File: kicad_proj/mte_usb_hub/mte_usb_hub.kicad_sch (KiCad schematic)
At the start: 22 parts

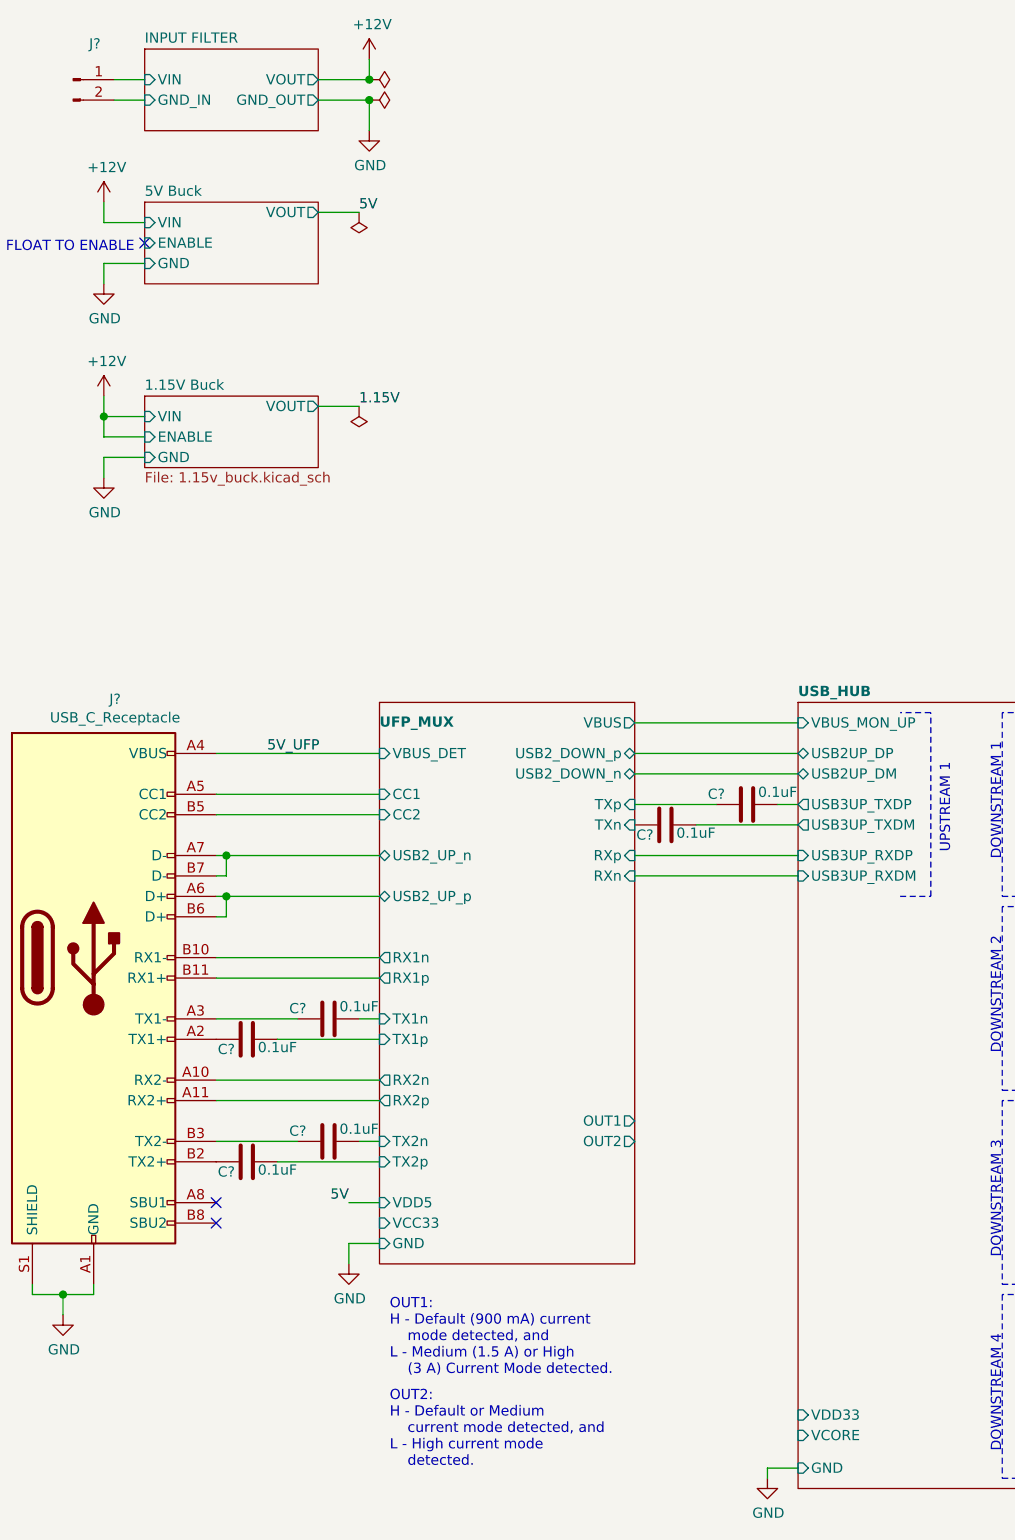
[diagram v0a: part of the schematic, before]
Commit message: Adds 3v3 LDO
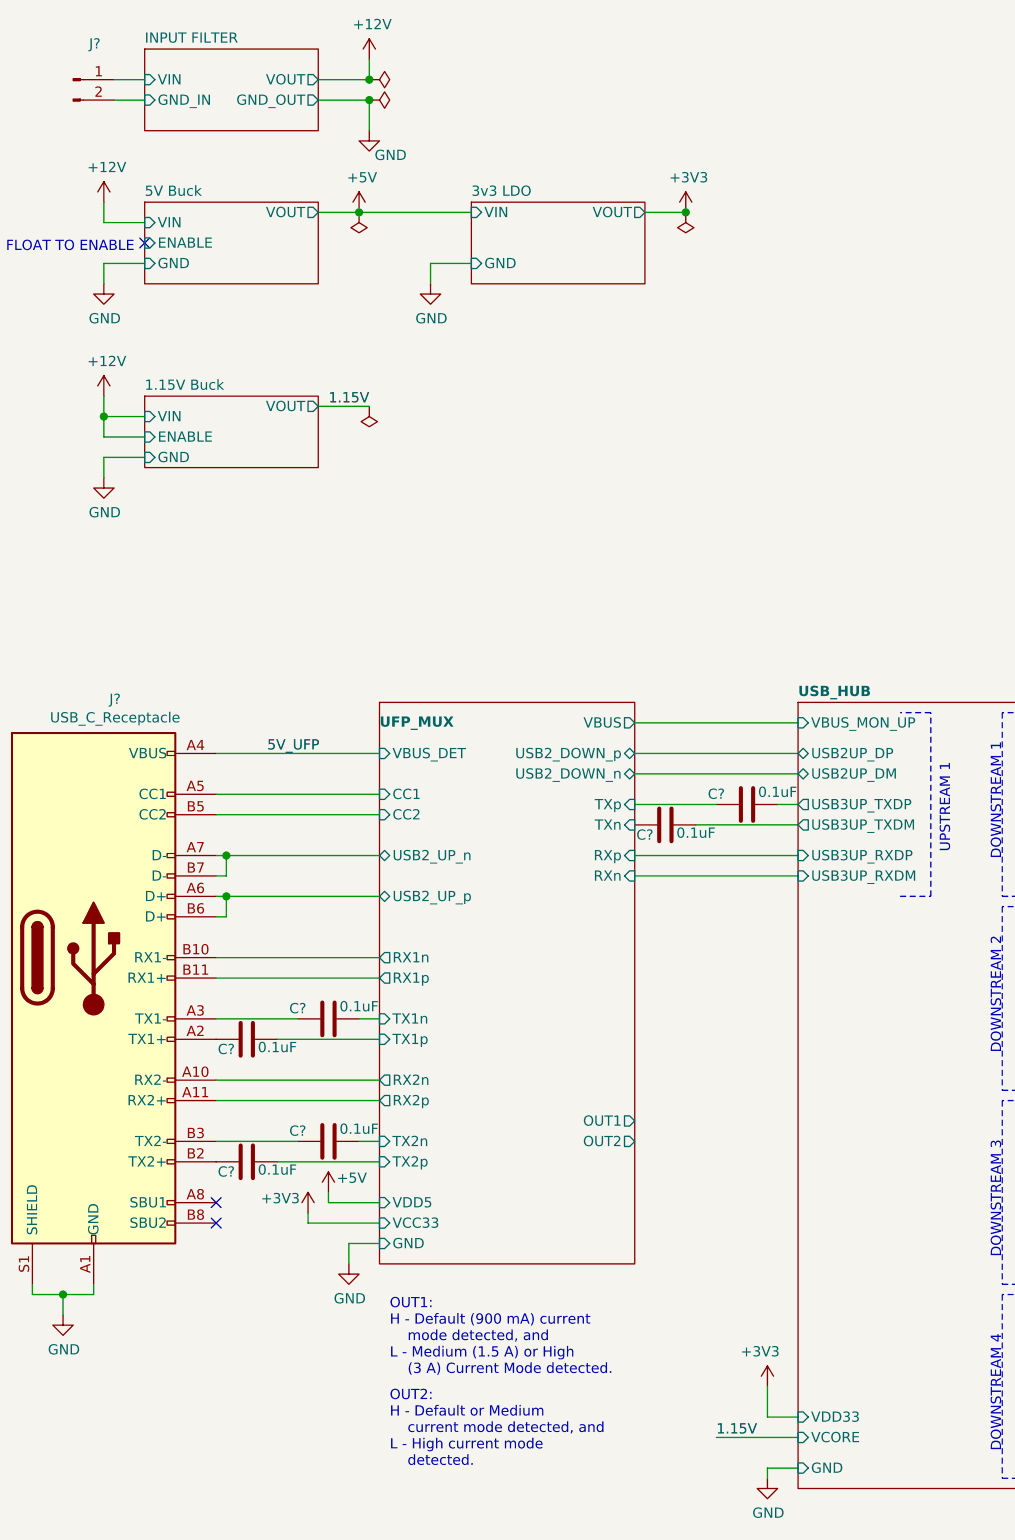
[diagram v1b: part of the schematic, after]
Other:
- added sheet 3v3 LDO (3v3_ldo.kicad_sch)

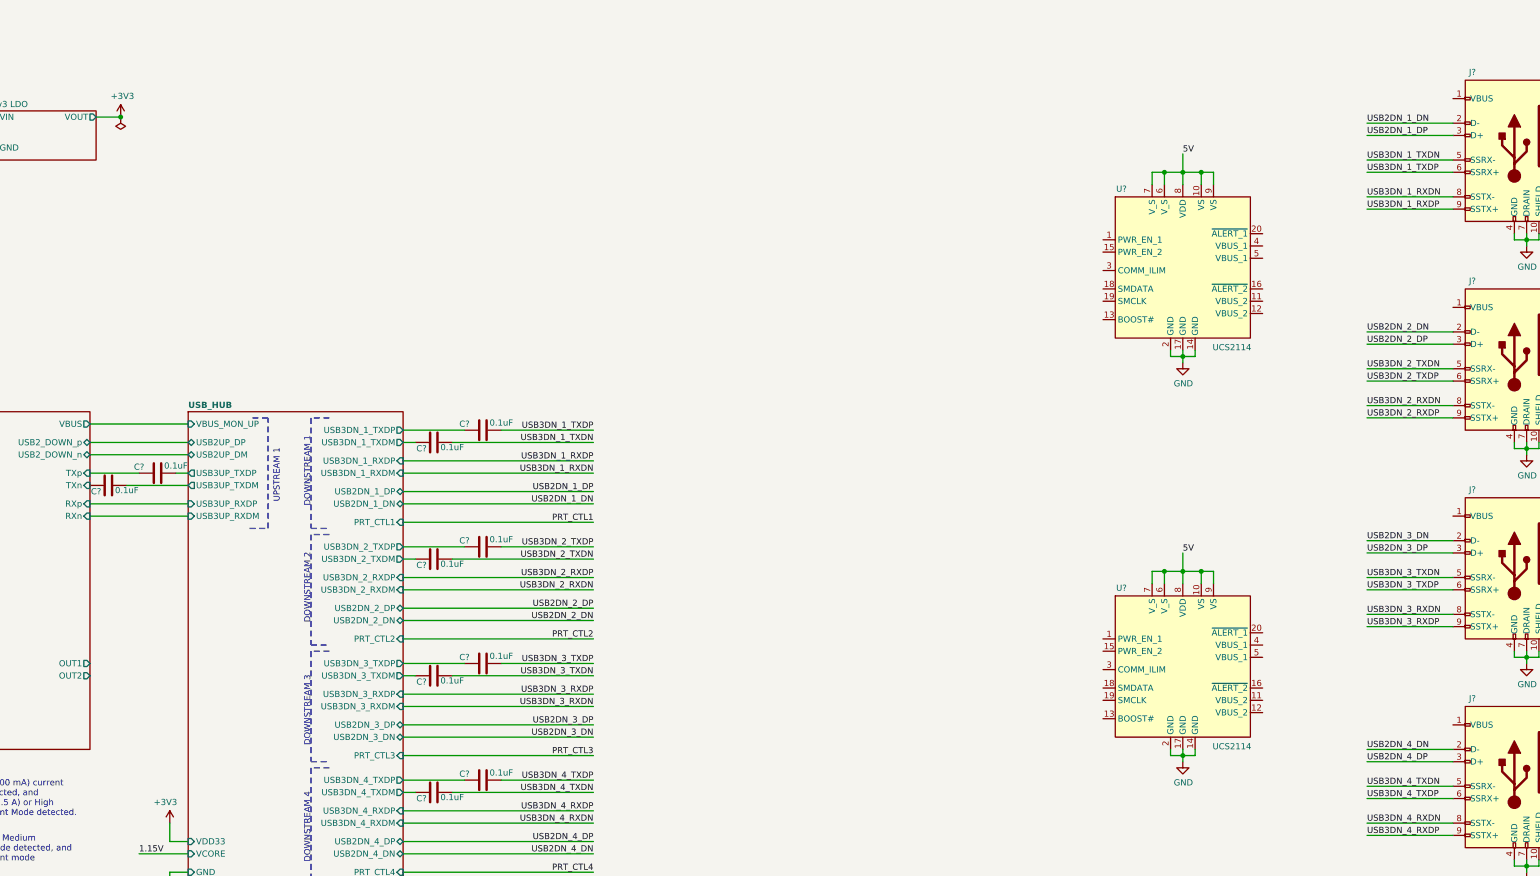
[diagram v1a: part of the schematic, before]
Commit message: Implements VBUS monitor, starts ESD protection
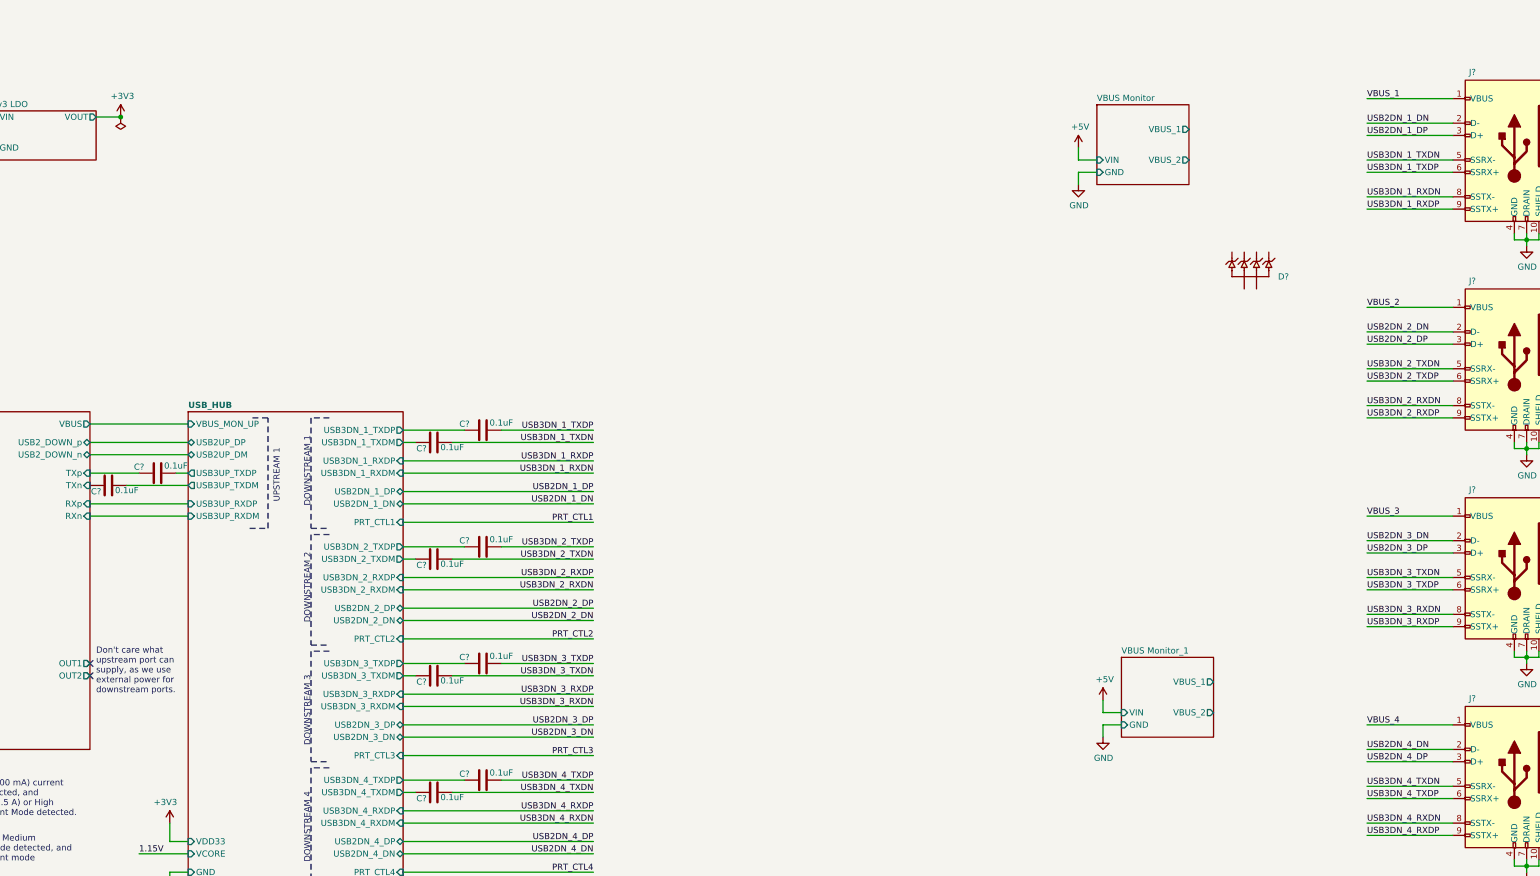
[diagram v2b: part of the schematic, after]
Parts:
- removed U? (x2): UCS2114, symbol mte_usb_hub:UCS2114
- added D?: ESD8004MUTAG, symbol mte_usb_hub:ESD8004MUTAG
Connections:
- net VBUS_3: now reaches J?.1 (VBUS)
- net VBUS_2: now reaches J?.1 (VBUS)
- net VBUS_1: now reaches J?.1 (VBUS)
- net VBUS_4: now reaches J?.1 (VBUS)
- no-connect marks 3 -> 5
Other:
- added sheet VBUS Monitor (vbus_monitor.kicad_sch)
- added sheet VBUS Monitor_1 (vbus_monitor.kicad_sch)
- note added: "Don't care what upstream port can supply, as we use external power for downstream ports."

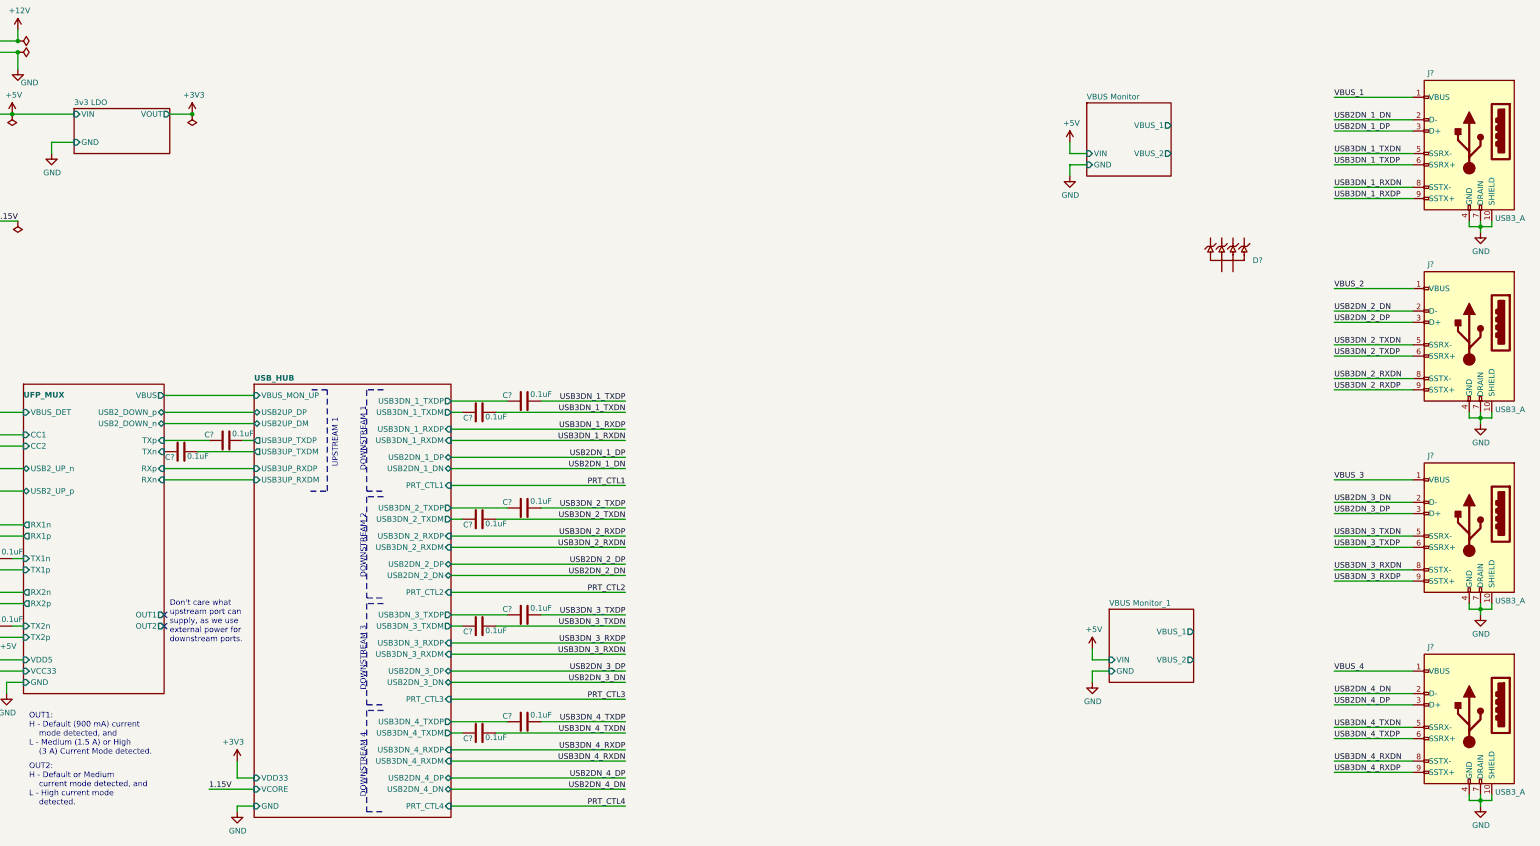
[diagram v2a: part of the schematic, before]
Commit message: Finishes input filter, minor buck changes
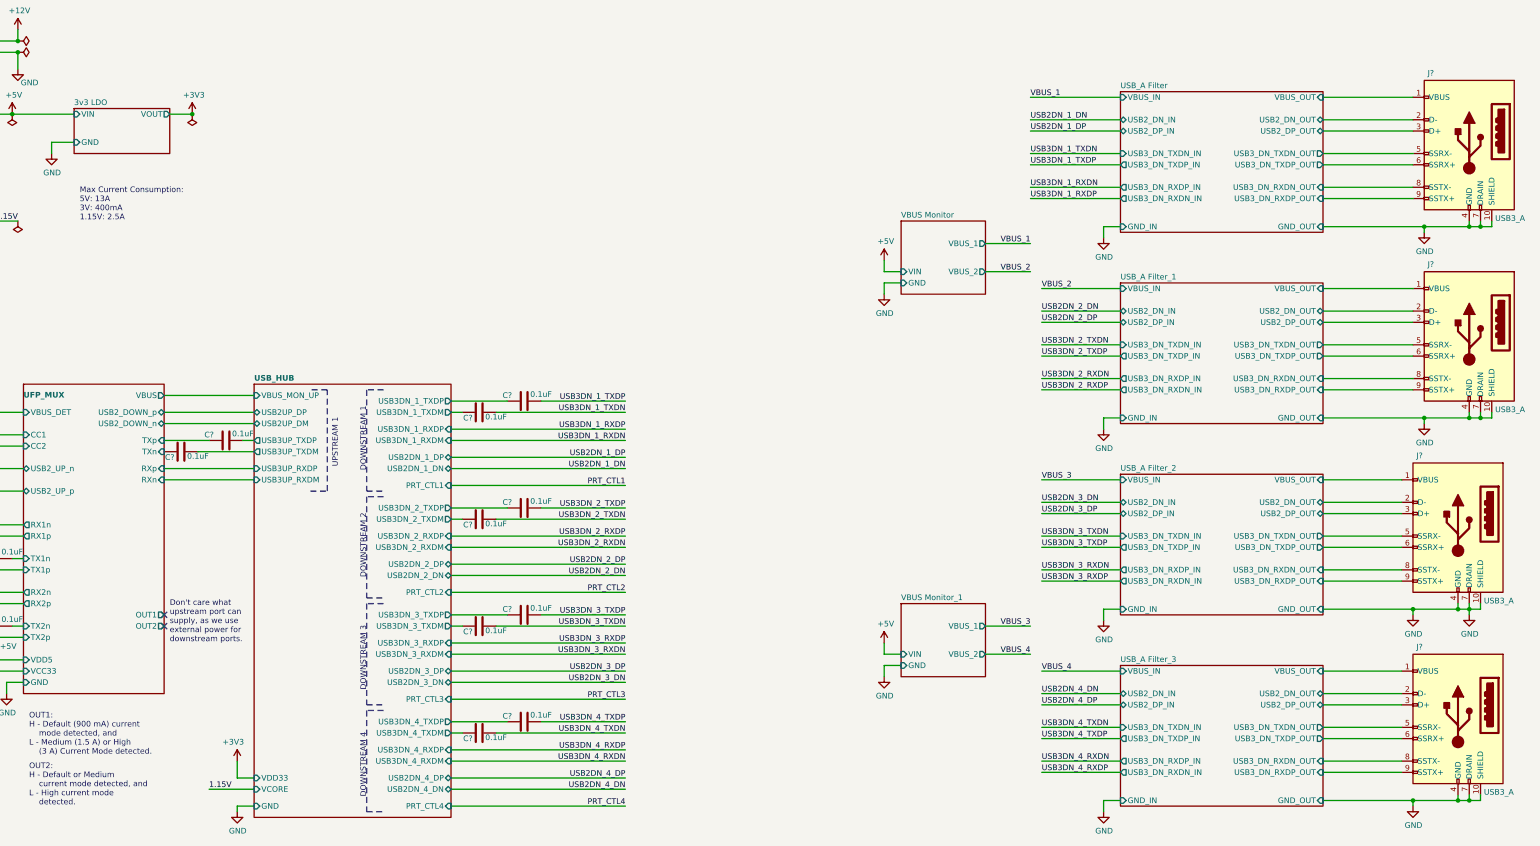
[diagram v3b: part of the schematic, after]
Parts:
- removed D?: ESD8004MUTAG, symbol mte_usb_hub:ESD8004MUTAG
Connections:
- net USB2DN_1_DN: no longer J?.2 (D-)
- net USB2DN_1_DP: no longer J?.3 (D+)
- net USB2DN_2_DN: no longer J?.2 (D-)
- net USB2DN_2_DP: no longer J?.3 (D+)
- net USB2DN_3_DN: no longer J?.2 (D-)
- net USB2DN_3_DP: no longer J?.3 (D+)
- net USB2DN_4_DN: no longer J?.2 (D-)
- net USB2DN_4_DP: no longer J?.3 (D+)
- net USB3DN_1_RXDN: no longer J?.8 (SSTX-)
- net USB3DN_1_RXDP: no longer J?.9 (SSTX+)
- net USB3DN_1_TXDN: no longer J?.5 (SSRX-)
- net USB3DN_1_TXDP: no longer J?.6 (SSRX+)
- net USB3DN_2_RXDN: no longer J?.8 (SSTX-)
- net USB3DN_2_RXDP: no longer J?.9 (SSTX+)
- net USB3DN_2_TXDN: no longer J?.5 (SSRX-)
- net USB3DN_2_TXDP: no longer J?.6 (SSRX+)
- net USB3DN_3_RXDN: no longer J?.8 (SSTX-)
- net USB3DN_3_RXDP: no longer J?.9 (SSTX+)
- net USB3DN_3_TXDN: no longer J?.5 (SSRX-)
- net USB3DN_3_TXDP: no longer J?.6 (SSRX+)
- net USB3DN_4_RXDN: no longer J?.8 (SSTX-)
- net USB3DN_4_RXDP: no longer J?.9 (SSTX+)
- net USB3DN_4_TXDN: no longer J?.5 (SSRX-)
- net USB3DN_4_TXDP: no longer J?.6 (SSRX+)
- net VBUS_1: no longer J?.1 (VBUS)
- net VBUS_2: no longer J?.1 (VBUS)
- net VBUS_3: no longer J?.1 (VBUS)
- net VBUS_4: no longer J?.1 (VBUS)
- new net USB_A Filter/USB2_DN_OUT: J?.2 (D-)
- new net USB_A Filter/USB2_DP_OUT: J?.3 (D+)
- new net USB_A Filter/USB3_DN_RXDN_OUT: J?.8 (SSTX-)
- new net USB_A Filter/USB3_DN_RXDP_OUT: J?.9 (SSTX+)
- new net USB_A Filter/USB3_DN_TXDN_OUT: J?.5 (SSRX-)
- new net USB_A Filter/USB3_DN_TXDP_OUT: J?.6 (SSRX+)
- new net USB_A Filter/VBUS_OUT: J?.1 (VBUS)
- new net USB_A Filter_1/USB2_DN_OUT: J?.2 (D-)
- new net USB_A Filter_1/USB2_DP_OUT: J?.3 (D+)
- new net USB_A Filter_1/USB3_DN_RXDN_OUT: J?.8 (SSTX-)
- new net USB_A Filter_1/USB3_DN_RXDP_OUT: J?.9 (SSTX+)
- new net USB_A Filter_1/USB3_DN_TXDN_OUT: J?.5 (SSRX-)
- new net USB_A Filter_1/USB3_DN_TXDP_OUT: J?.6 (SSRX+)
- new net USB_A Filter_1/VBUS_OUT: J?.1 (VBUS)
- new net USB_A Filter_2/USB2_DN_OUT: J?.2 (D-)
- new net USB_A Filter_2/USB2_DP_OUT: J?.3 (D+)
- new net USB_A Filter_2/USB3_DN_RXDN_OUT: J?.8 (SSTX-)
- new net USB_A Filter_2/USB3_DN_RXDP_OUT: J?.9 (SSTX+)
- new net USB_A Filter_2/USB3_DN_TXDN_OUT: J?.5 (SSRX-)
- new net USB_A Filter_2/USB3_DN_TXDP_OUT: J?.6 (SSRX+)
- new net USB_A Filter_2/VBUS_OUT: J?.1 (VBUS)
- new net USB_A Filter_3/USB2_DN_OUT: J?.2 (D-)
- new net USB_A Filter_3/USB2_DP_OUT: J?.3 (D+)
- new net USB_A Filter_3/USB3_DN_RXDN_OUT: J?.8 (SSTX-)
- new net USB_A Filter_3/USB3_DN_RXDP_OUT: J?.9 (SSTX+)
- new net USB_A Filter_3/USB3_DN_TXDN_OUT: J?.5 (SSRX-)
- new net USB_A Filter_3/USB3_DN_TXDP_OUT: J?.6 (SSRX+)
- new net USB_A Filter_3/VBUS_OUT: J?.1 (VBUS)
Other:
- added sheet USB_A Filter (usb_a_filter.kicad_sch)
- added sheet USB_A Filter_1 (usb_a_filter.kicad_sch)
- added sheet USB_A Filter_2 (usb_a_filter.kicad_sch)
- added sheet USB_A Filter_3 (usb_a_filter.kicad_sch)
- note added: "Max Current Consumption: 5V: 13A 3V: 400mA 1.15V: 2.5A"
- moved on the sheet: J?

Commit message: Updates input protection, output BC enabled
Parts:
- gave numbers to parts that had none: 20
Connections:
- net 5V_UFP: no longer J2.A4 (VBUS), J2.A9 (VBUS), J2.B4 (VBUS), J2.B9 (VBUS)
- net UFP_MUX/CC1: no longer J2.A5 (CC1)
- net UFP_MUX/CC2: no longer J2.B5 (CC2)
- net UFP_MUX/RX1n: no longer J2.B10 (RX1-)
- net UFP_MUX/RX1p: no longer J2.B11 (RX1+)
- net UFP_MUX/RX2n: no longer J2.A10 (RX2-)
- net UFP_MUX/RX2p: no longer J2.A11 (RX2+)
- net UFP_MUX/USB2_UP_n: no longer J2.A7 (D-), J2.B7 (D-)
- net UFP_MUX/USB2_UP_p: no longer J2.A6 (D+), J2.B6 (D+)
- net USB_C Filter/TX2+_IN: now reaches J2.B2 (TX2+)
- net USB_C Filter/TX2+_IN: no longer C2.1
- net USB_C Filter/TX1-_IN: now reaches J2.A3 (TX1-)
- net USB_C Filter/TX1-_IN: no longer C3.1
- net USB_C Filter/TX1+_IN: now reaches J2.A2 (TX1+)
- net USB_C Filter/TX1+_IN: no longer C1.1
- net USB_C Filter/TX2-_IN: now reaches J2.B3 (TX2-)
- net USB_C Filter/TX2-_IN: no longer C4.1
- new net USB_C Filter/CC1_IN: J2.A5 (CC1)
- new net USB_C Filter/CC2_IN: J2.B5 (CC2)
- new net USB_C Filter/D+_IN: J2.A6 (D+), J2.B6 (D+)
- new net USB_C Filter/D-_IN: J2.A7 (D-), J2.B7 (D-)
- new net USB_C Filter/RX1+_IN: J2.B11 (RX1+)
- new net USB_C Filter/RX1-_IN: J2.B10 (RX1-)
- new net USB_C Filter/RX2+_IN: J2.A11 (RX2+)
- new net USB_C Filter/RX2-_IN: J2.A10 (RX2-)
- new net USB_C Filter/TX1+_OUT: C1.1
- new net USB_C Filter/TX1-_OUT: C3.1
- new net USB_C Filter/TX2+_OUT: C2.1
- new net USB_C Filter/TX2-_OUT: C4.1
- new net USB_C Filter/VBUS_IN: J2.A4 (VBUS), J2.A9 (VBUS), J2.B4 (VBUS), J2.B9 (VBUS)
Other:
- added sheet USB_C Filter (usb_c_filter.kicad_sch)
- moved on the sheet: C1, C10, C11, C12, C13, C14, C2, C3, C4, C5, C6, C7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
